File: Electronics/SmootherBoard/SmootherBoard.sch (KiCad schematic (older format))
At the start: 36 parts, among them SW1 SW_Push, SW2 SW_Push, U1 WeMos_D1_mini, U10 CNY70, U2 MPU6050_breakdown, U3 PCA9685PW, U4 TP4056_module, U5 CNY70, U6 CNY70, U7 DRV8833_module, U8 DRV8833_module, U9 CNY70

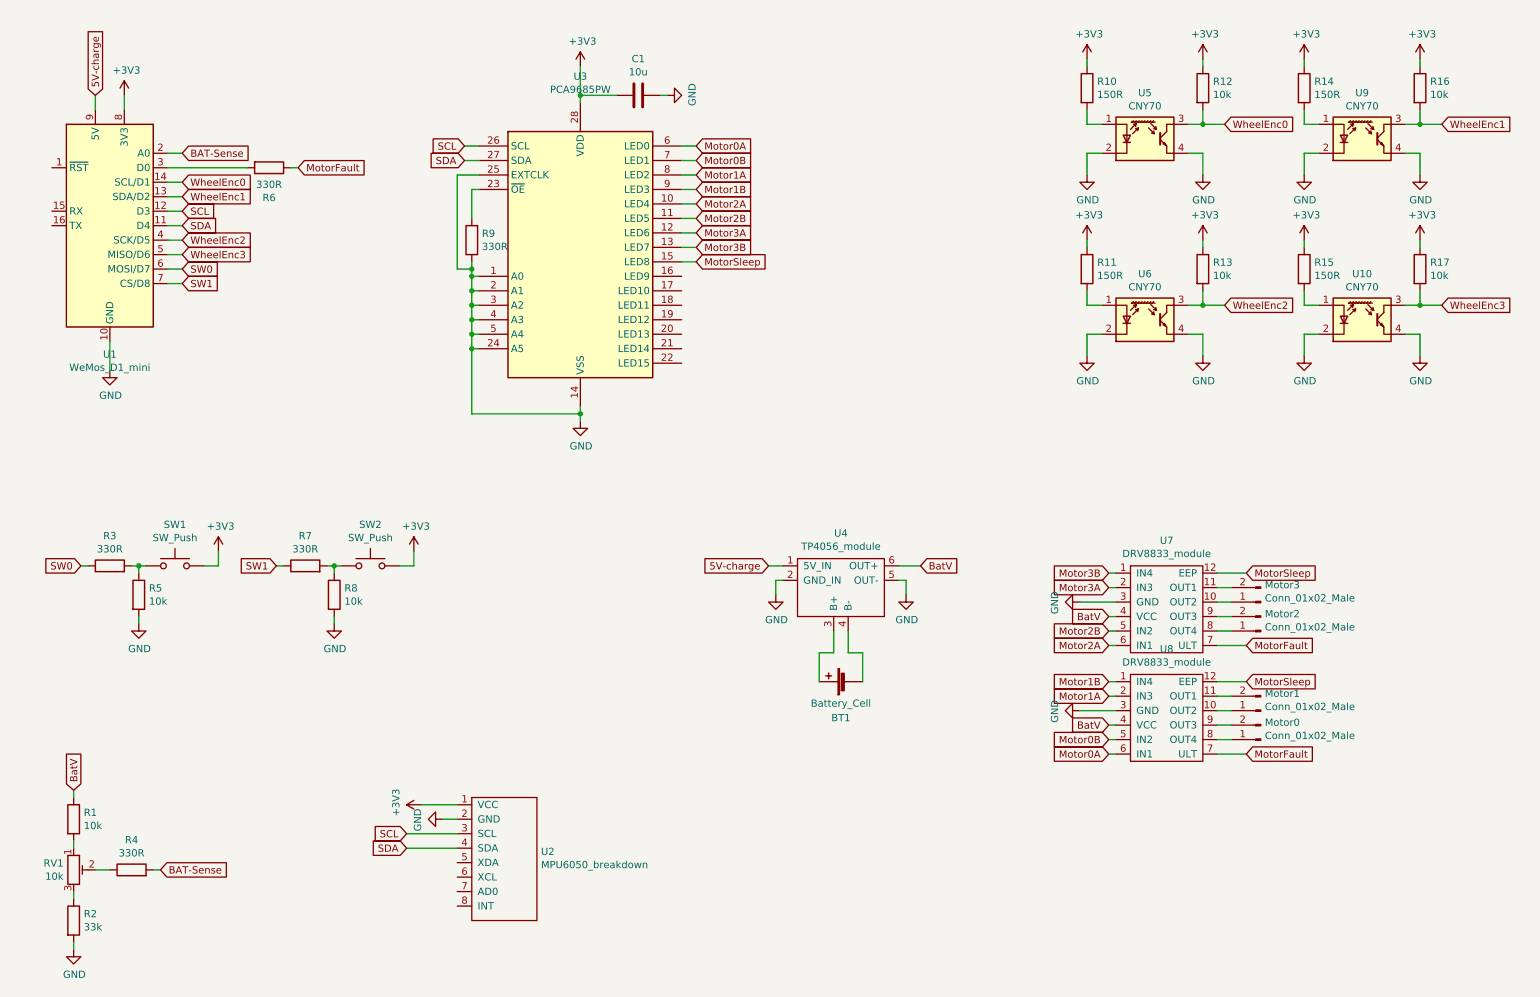
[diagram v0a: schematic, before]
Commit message: Changed for ESP32. Added signature, 3V3 LDR.
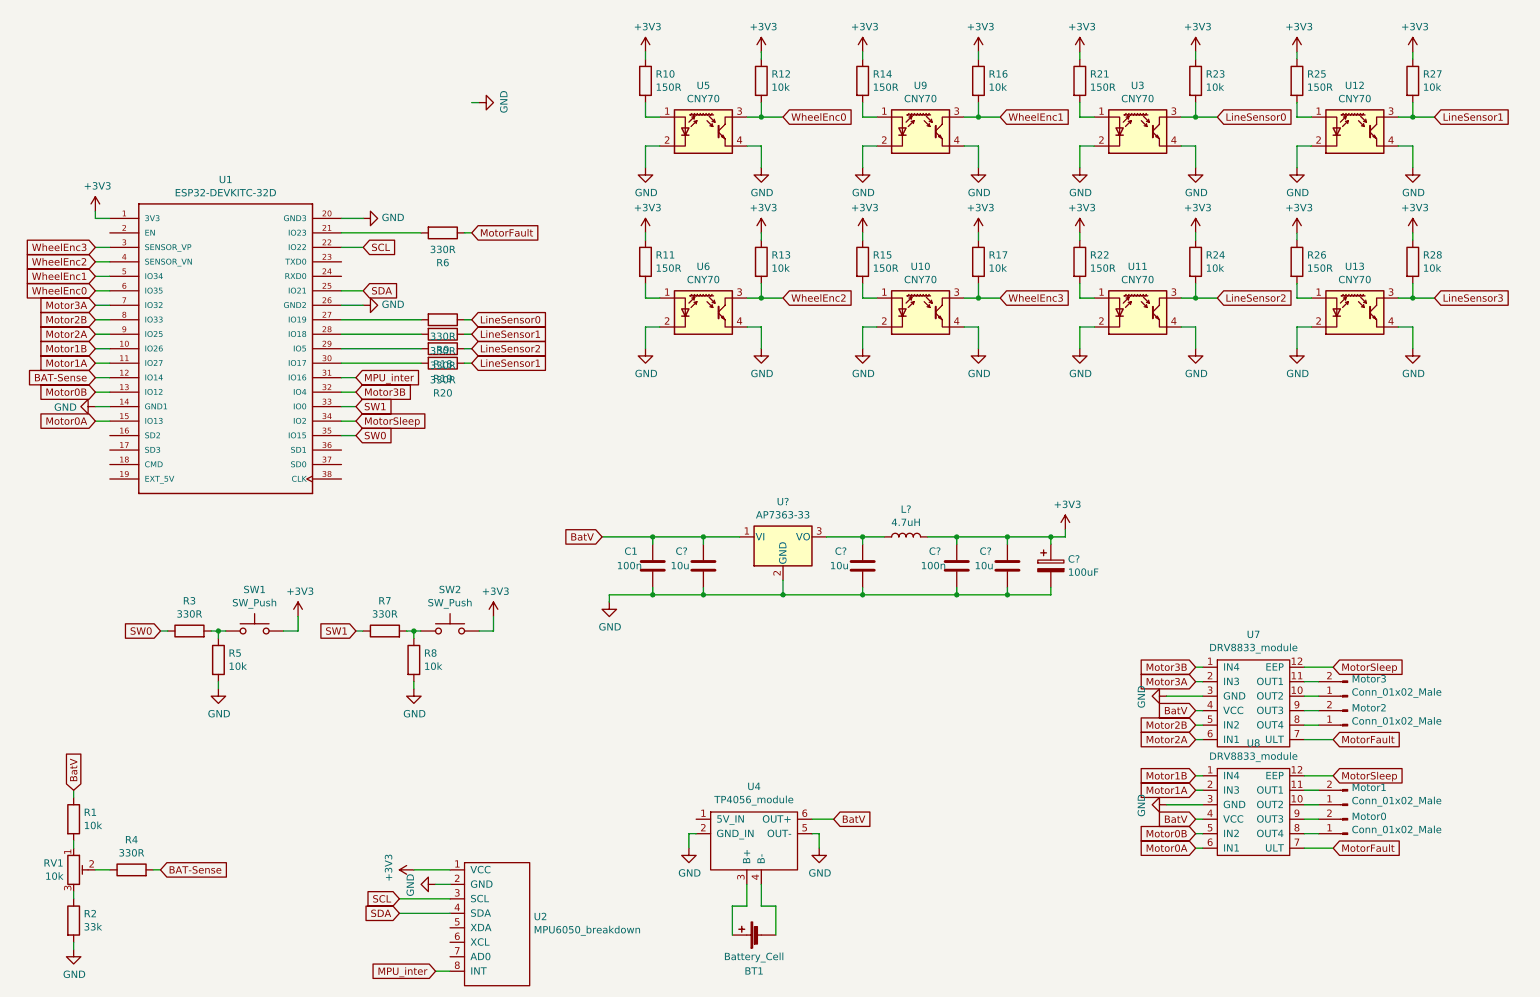
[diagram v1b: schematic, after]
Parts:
- removed U1: WeMos_D1_mini, Module:WEMOS_D1_mini_light, symbol MCU_Module:WeMos_D1_mini
- removed U3: PCA9685PW, Package_SO:TSSOP-28_4.4x9.7mm_P0.65mm, symbol Driver_LED:PCA9685PW
- added C? (x3): 10u, Capacitor_SMD:C_1206_3216Metric_Pad1.42x1.75mm_HandSolder, symbol Device:C
- added C?: 100n, Capacitor_SMD:C_1206_3216Metric_Pad1.42x1.75mm_HandSolder, symbol Device:C
- added C?: 100uF, Capacitor_THT:CP_Radial_D8.0mm_P3.50mm, symbol Device:CP
- added L?: 4.7uH, Inductor_SMD:L_1206_3216Metric, symbol Device:L
- added R18, R19, R20: 330R, Resistor_SMD:R_1206_3216Metric_Pad1.42x1.75mm_HandSolder, symbol Device:R
- added R21, R22, R25, R26: 150R, Resistor_SMD:R_1206_3216Metric_Pad1.42x1.75mm_HandSolder, symbol Device:R
- added R23, R24, R27, R28: 10k, Resistor_SMD:R_1206_3216Metric_Pad1.42x1.75mm_HandSolder, symbol Device:R
- added U1: ESP32-DEVKITC-32D, SmootherBoard:MODULE_ESP32-DEVKITC-32D, symbol ESP32-DEVKITC-32D:ESP32-DEVKITC-32D
- added U11, U12, U13, U3: CNY70, OptoDevice:Vishay_CNY70, symbol Sensor_Proximity:CNY70
- added U?: AP7363-33, Package_TO_SOT_SMD:SOT-223-3_TabPin2, symbol Regulator_Linear:AP7361C-33E
- C1: value 10u -> 100n
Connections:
- net +3V3: now also C?.1, C?.1, C?.1, L?.2, R21.1, R22.1, R23.1, R24.1, R25.1, R26.1, R27.1, R28.1, U1.1 (3V3); no longer C1.2
- net BAT-Sense: now also U1.12 (IO14)
- net BatV: now also C1.1, C?.1, U?.1 (VI)
- net GND: now also C1.2, C?.2, C?.2, C?.2, C?.2, C?.2, U1.14 (GND1), U1.20 (GND3), U1.26 (GND2), U11.2 (K), U11.4 (E), U12.2 (K), U12.4 (E), U13.2 (K), U13.4 (E), U3.2 (K), U3.4 (E), U?.2 (GND); no longer C1.1, R9.1
- net Motor0A: now also U1.15 (IO13)
- net Motor0B: now also U1.13 (IO12)
- net Motor1A: now also U1.11 (IO27)
- net Motor1B: now also U1.10 (IO26)
- net Motor2A: now also U1.9 (IO25)
- net Motor2B: now also U1.8 (IO33)
- net Motor3A: now also U1.7 (IO32)
- net Motor3B: now also U1.32 (IO4)
- net MotorSleep: now also U1.34 (IO2)
- net SCL: now also U1.22 (IO22)
- net SDA: now also U1.25 (IO21)
- net SW0: now also U1.35 (IO15)
- net SW1: now also U1.33 (IO0)
- net WheelEnc0: now also U1.6 (IO35)
- net WheelEnc1: now also U1.5 (IO34)
- net WheelEnc2: now also U1.4 (SENSOR_VN)
- net WheelEnc3: now also U1.3 (SENSOR_VP)
- net at R9.2: now also U1.27 (IO19)
- net at R6.2: now also U1.21 (IO23)
- net MPU_inter: now reaches U2.8 (INT)
- net MPU_inter: now also U1.31 (IO16)
- net 5V-charge: no longer names the net of U4.1 (5V_IN)
- new net: R18.2, U1.28 (IO18)
- new net: R19.2, U1.29 (IO5)
- new net: R20.2, U1.30 (IO17)
- new net: R21.2, U3.1 (A)
- new net: R25.2, U12.1 (A)
- new net: R22.2, U11.1 (A)
- new net: R26.2, U13.1 (A)
- new net: C?.1, L?.1, U?.3 (VO)
- new net LineSensor0: R23.2, R9.1, U3.3 (C)
- new net LineSensor1: R18.1, R20.1, R27.2, U12.3 (C)
- new net LineSensor2: R19.1, R24.2, U11.3 (C)
- new net LineSensor3: R28.2, U13.3 (C)
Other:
- moved on the sheet: BT1, C1, Motor0, Motor1, Motor2, Motor3, R10, R11, R12, R13, R14, R15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

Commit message: Generated manufacturing files.
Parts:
- added J?: Conn_01x02_Male, Connector_PinHeader_2.54mm:PinHeader_1x02_P2.54mm_Vertical, symbol Connector:Conn_01x02_Male
- gave numbers to parts that had none: 7
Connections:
- net BatV: now also J?.1 (Pin_1); no longer U4.6 (OUT+)
- new net: J?.2 (Pin_2), U4.6 (OUT+)
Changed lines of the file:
@@
 	1    0    0    -1
 $EndComp
-Text GLabel 6450 6150 2    50   Input ~ 0
+Text GLabel 6750 6150 2    50   Input ~ 0
 BatV
 Wire Wire Line
@@
 $EndComp
 $Comp
-L power:GND #PWR0127
-U 1 1 5E7F456E
-P 4000 1200
-F 0 "#PWR0127" H 4000 950 50  0001 C CNN
-F 1 "GND" H 4005 1027 50  0000 C CNN
-F 2 "" H 4000 1200 50  0001 C CNN
-F 3 "" H 4000 1200 50  0001 C CNN
-	1    4000 1200
-	0    -1   -1   0
-$EndComp
-Wire Wire Line
-	4000 1200 3950 1200
-$Comp
 L Device:R R1
 U 1 1 5E819083
@@
 BatV
 $Comp
-L power:GND #PWR?
+L power:GND #PWR0149
 U 1 1 5EC733A1
 P 4900 4650
-F 0 "#PWR?" H 4900 4400 50  0001 C CNN
+F 0 "#PWR0149" H 4900 4400 50  0001 C CNN
 F 1 "GND" H 4905 4477 50  0000 C CNN
 F 2 "" H 4900 4650 50  0001 C CNN
@@
 $EndComp
 $Comp
-L Device:C C?
+L Device:C C2
 U 1 1 5EC9C393
 P 5550 4400
-F 0 "C?" H 5400 4500 50  0000 C CNN
+F 0 "C2" H 5400 4500 50  0000 C CNN
 F 1 "10u" H 5389 4400 50  0000 C CNN
 F 2 "Capacitor_SMD:C_1206_3216Metric_Pad1.42x1.75mm_HandSolder" H 5588 4250 50  0001 C CNN
@@
 Connection ~ 5200 4200
 $Comp
-L Regulator_Linear:AP7361C-33E U?
+L Regulator_Linear:AP7361C-33E U14
 U 1 1 5ECD3BE7
 P 6100 4200
-F 0 "U?" H 6100 4442 50  0000 C CNN
+F 0 "U14" H 6100 4442 50  0000 C CNN
 F 1 "AP7363-33" H 6100 4351 50  0000 C CNN
 F 2 "Package_TO_SOT_SMD:SOT-223-3_TabPin2" H 6100 4425 50  0001 C CIN
@@
 Connection ~ 5550 4600
 $Comp
-L Device:C C?
+L Device:C C3
 U 1 1 5ECED28E
 P 6650 4400
-F 0 "C?" H 6500 4500 50  0000 C CNN
+F 0 "C3" H 6500 4500 50  0000 C CNN
 F 1 "10u" H 6489 4400 50  0000 C CNN
 F 2 "Capacitor_SMD:C_1206_3216Metric_Pad1.42x1.75mm_HandSolder" H 6688 4250 50  0001 C CNN
@@
 $EndComp
 $Comp
-L Device:C C?
+L Device:C C4
 U 1 1 5ECF8BEB
 P 7300 4400
-F 0 "C?" H 7150 4500 50  0000 C CNN
+F 0 "C4" H 7150 4500 50  0000 C CNN
 F 1 "100n" H 7139 4400 50  0000 C CNN
 F 2 "Capacitor_SMD:C_1206_3216Metric_Pad1.42x1.75mm_HandSolder" H 7338 4250 50  0001 C CNN
@@
 Connection ~ 6100 4600
 $Comp
-L Device:L L?
+L Device:L L1
 U 1 1 5ED1CA5E
 P 6950 4200
-F 0 "L?" V 7140 4200 50  0000 C CNN
+F 0 "L1" V 7140 4200 50  0000 C CNN
 F 1 "4.7uH" V 7049 4200 50  0000 C CNN
 F 2 "Inductor_SMD:L_1206_3216Metric" H 6950 4200 50  0001 C CNN
@@
 Connection ~ 6650 4600
 $Comp
-L Device:C C?
+L Device:C C5
 U 1 1 5ED43AEA
 P 7650 4400
-F 0 "C?" H 7500 4500 50  0000 C CNN
+F 0 "C5" H 7500 4500 50  0000 C CNN
 F 1 "10u" H 7489 4400 50  0000 C CNN
 F 2 "Capacitor_SMD:C_1206_3216Metric_Pad1.42x1.75mm_HandSolder" H 7688 4250 50  0001 C CNN
@@
 Connection ~ 7300 4600
 $Comp
-L Device:CP C?
+L Device:CP C6
 U 1 1 5ED6AFDC
 P 7950 4400
-F 0 "C?" H 8068 4446 50  0000 L CNN
+F 0 "C6" H 8068 4446 50  0000 L CNN
 F 1 "100uF" H 8068 4355 50  0000 L CNN
 F 2 "Capacitor_THT:CP_Radial_D8.0mm_P3.50mm" H 7988 4250 50  0001 C CNN
@@
 Connection ~ 7650 4600
 $Comp
-L power:+3V3 #PWR?
+L power:+3V3 #PWR0150
 U 1 1 5ED9602E
 P 8050 4150
-F 0 "#PWR?" H 8050 4000 50  0001 C CNN
+F 0 "#PWR0150" H 8050 4000 50  0001 C CNN
 F 1 "+3V3" H 8065 4323 50  0000 C CNN
 F 2 "" H 8050 4150 50  0001 C CNN
@@
 	8050 4200 8050 4150
 Connection ~ 7950 4200
+$Comp
+L Connector:Conn_01x02_Male J?
+U 1 1 5EE83C64
+P 6550 5950
+F 0 "J?" V 6612 5994 50  0000 L CNN
+F 1 "Conn_01x02_Male" V 6703 5994 50  0000 L CNN
+F 2 "Connector_PinHeader_2.54mm:PinHeader_1x02_P2.54mm_Vertical" H 6550 5950 50  0001 C CNN
+F 3 "~" H 6550 5950 50  0001 C CNN
+	1    6550 5950
+	0    1    1    0
+$EndComp
+Wire Wire Line
+	6550 6150 6750 6150
 $EndSCHEMATC

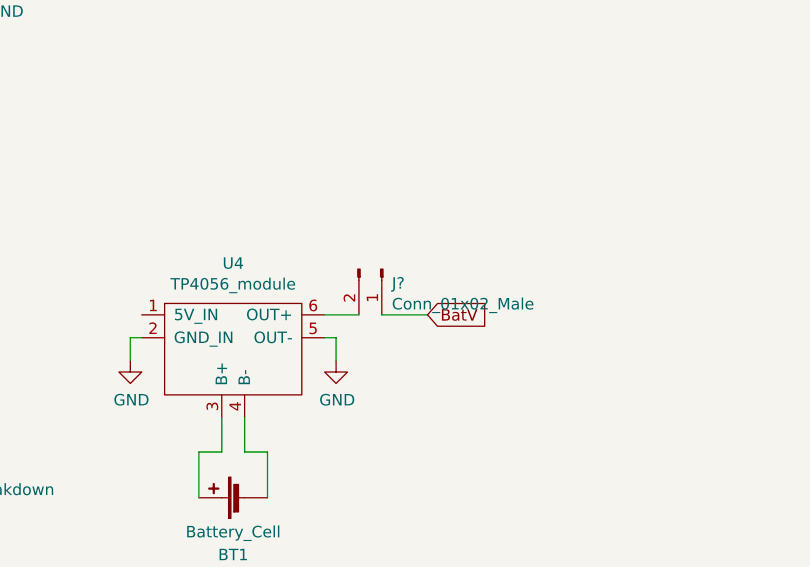
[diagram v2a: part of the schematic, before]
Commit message: Changed LDO package for sot-252.
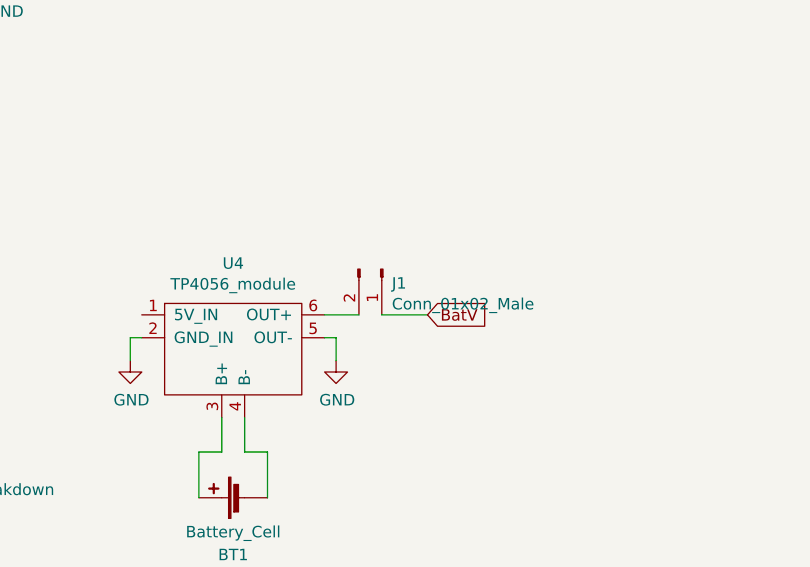
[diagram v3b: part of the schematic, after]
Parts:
- U14: footprint Package_TO_SOT_SMD:SOT-223-3_TabPin2 -> Package_TO_SOT_SMD:TO-252-3_TabPin2
- gave numbers to parts that had none: 1
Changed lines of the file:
@@
 F 0 "U14" H 6100 4442 50  0000 C CNN
 F 1 "AP7363-33" H 6100 4351 50  0000 C CNN
-F 2 "Package_TO_SOT_SMD:SOT-223-3_TabPin2" H 6100 4425 50  0001 C CIN
+F 2 "Package_TO_SOT_SMD:TO-252-3_TabPin2" H 6100 4425 50  0001 C CIN
 F 3 "https://www.diodes.com/assets/Datasheets/AP7361C.pdf" H 6100 4150 50  0001 C CNN
 	1    6100 4200
@@
 Connection ~ 7950 4200
 $Comp
-L Connector:Conn_01x02_Male J?
+L Connector:Conn_01x02_Male J1
 U 1 1 5EE83C64
 P 6550 5950
-F 0 "J?" V 6612 5994 50  0000 L CNN
+F 0 "J1" V 6612 5994 50  0000 L CNN
 F 1 "Conn_01x02_Male" V 6703 5994 50  0000 L CNN
 F 2 "Connector_PinHeader_2.54mm:PinHeader_1x02_P2.54mm_Vertical" H 6550 5950 50  0001 C CNN
